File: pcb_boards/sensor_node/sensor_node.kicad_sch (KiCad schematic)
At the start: 58 parts, among them IC1 PCF2129T, J1 Screw_Terminal_01x15, J2 Conn_02x03_Odd_Even, J3 USB_B_Micro, J4 Screw_Terminal_01x12, U1 SiP32431, U2 ESP32-WROOM-32, U3 RF-LORA-868-SO, U4 FT232RL, U7 RP604x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

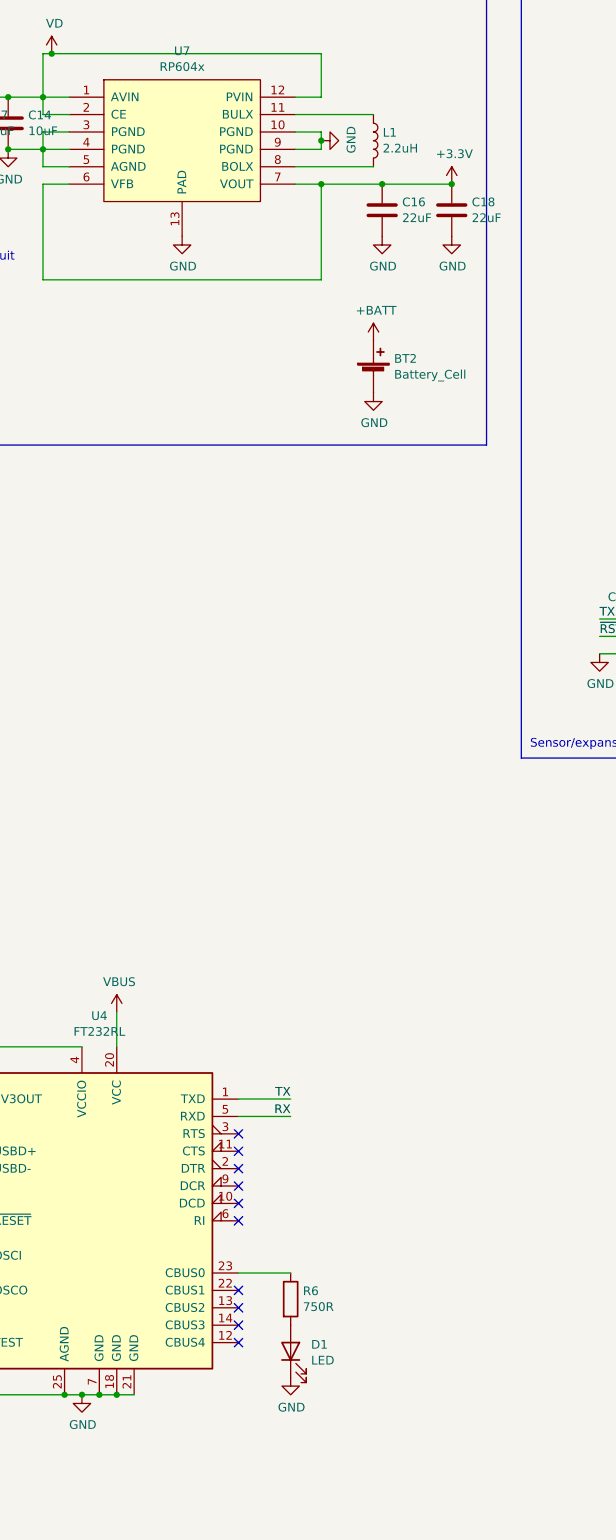
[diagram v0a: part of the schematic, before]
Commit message: Switch USB programmer UART lines; fix LED
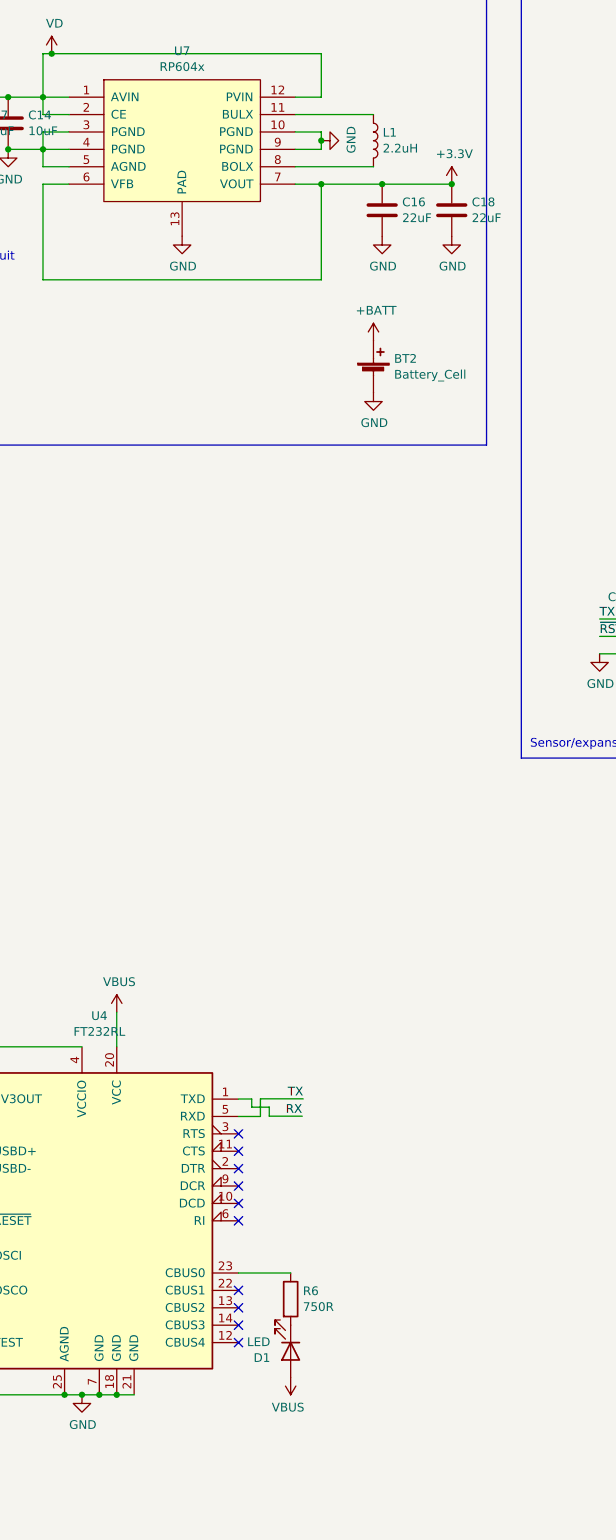
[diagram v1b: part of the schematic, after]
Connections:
- net GND: no longer D1.1 (K)
- net RX: now also U4.1 (TXD); no longer U4.5 (RXD)
- net TX: now also U4.5 (RXD); no longer U4.1 (TXD)
- net VBUS: now also D1.2 (A)
- net at R6.2: now also D1.1 (K); no longer D1.2 (A)
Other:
- moved on the sheet: D1

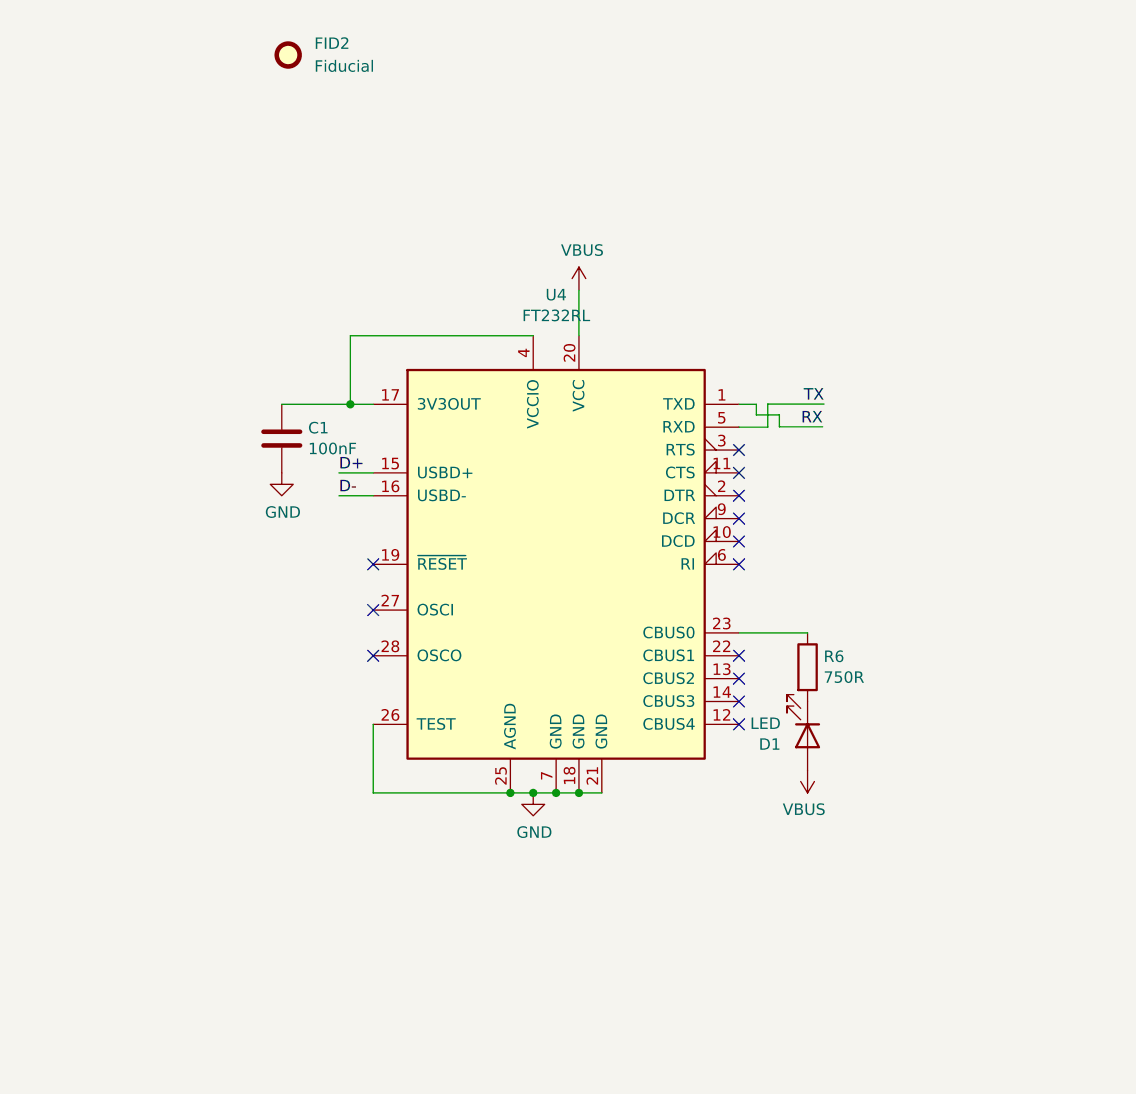
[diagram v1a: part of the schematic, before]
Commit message: Make USB connector vertical; fix tiny errors
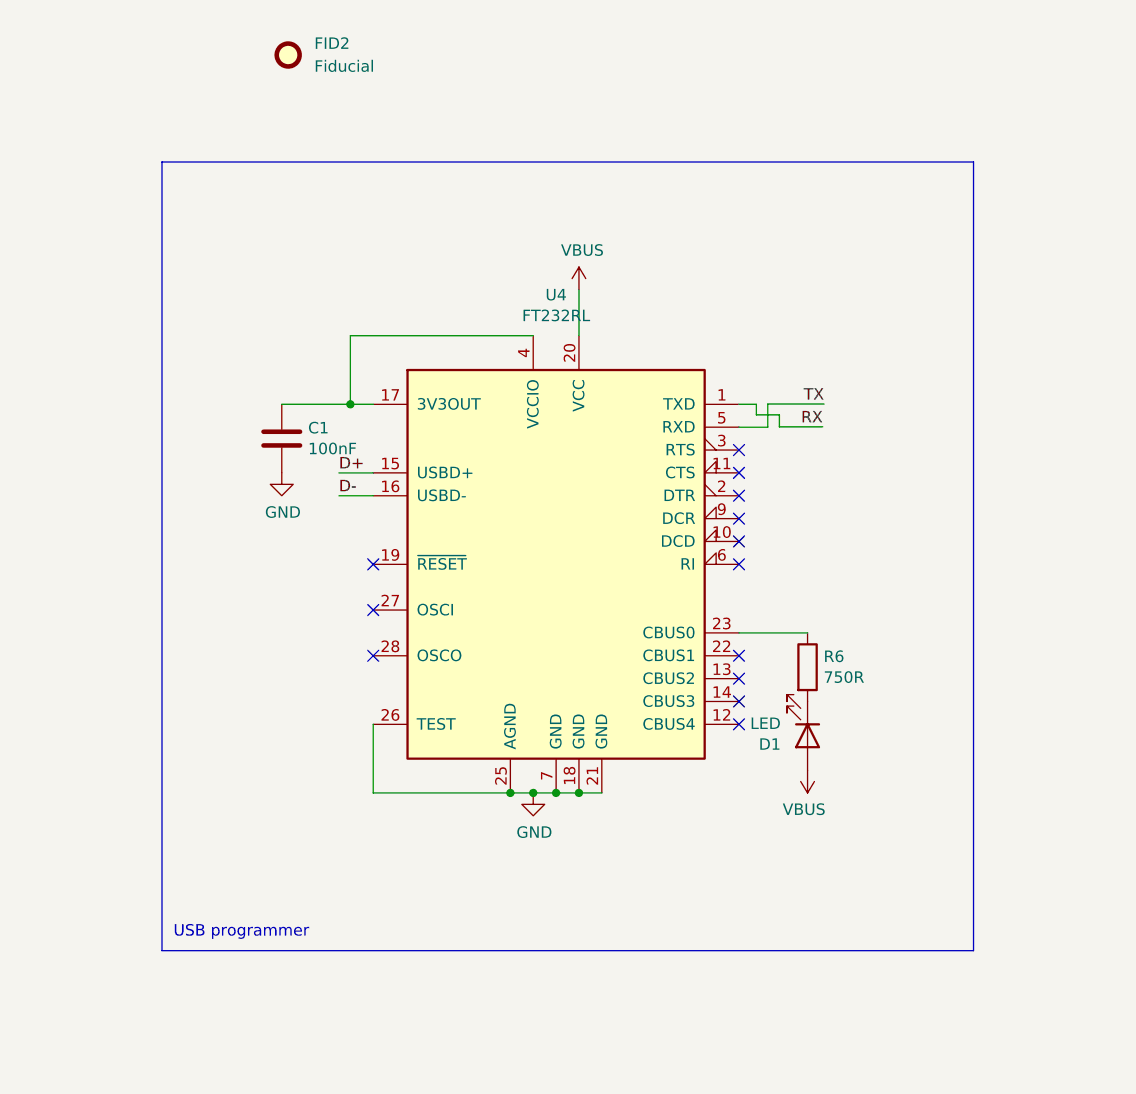
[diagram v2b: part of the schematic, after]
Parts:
- J3: footprint Connector_USB:USB_Micro-B_Molex-105017-0001 -> Connector_USB:USB_Micro-B_Molex-105133-0001
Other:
- note added: "USB programmer"
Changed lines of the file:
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@@
+    (stroke (width 0) (type default))
+  )
+  (polyline (pts (xy 265.43 149.86) (xy 265.43 237.49))
     (stroke (width 0) (type default))
   )
@@
     (stroke (width 0) (type default))
   )
+  (polyline (pts (xy 175.26 149.86) (xy 265.43 149.86))
+    (stroke (width 0) (type default))
+  )
   (polyline (pts (xy 16.51 143.51) (xy 74.93 143.51))
     (stroke (width 0) (type default))
@@
     (stroke (width 0) (type default))
   )
+  (polyline (pts (xy 175.26 149.86) (xy 175.26 237.49))
+    (stroke (width 0) (type default))
+  )
   (wire (pts (xy 78.74 24.13) (xy 78.74 30.48))
     (stroke (width 0) (type default))
@@
     (stroke (width 0) (type default))
   )
+  (polyline (pts (xy 175.26 237.49) (xy 265.43 237.49))
+    (stroke (width 0) (type default))
+  )
   (wire (pts (xy 373.38 214.63) (xy 388.62 214.63))
     (stroke (width 0) (type default))
@@
   )
   (text "Power switch" (at 17.78 142.24 0)
+    (effects (font (size 1.27 1.27)) (justify left bottom))
+  )
+  (text "USB programmer" (at 176.53 236.22 0)
     (effects (font (size 1.27 1.27)) (justify left bottom))
   )
@@
       (effects (font (size 1.27 1.27)))
     )
-    (property "Footprint" "Connector_USB:USB_Micro-B_Molex-105017-0001" (at 167.64 33.02 0)
-      (effects (font (size 1.27 1.27)) hide)
-    )
+    (property "Footprint" "Connector_USB:USB_Micro-B_Molex-105133-0001" (at 167.64 33.02 0)
+      (effects (font (size 1.27 1.27)) hide)
+    )
